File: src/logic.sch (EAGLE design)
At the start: 70 parts, among them CON1 CON-4P-TABS-JST_GH-RA, CON11 PINHEAD_1X04-2, CON12 PINHEAD_1X04-2, CON2 PINHEAD_1X04-2.54, CON3 PINHEAD_2X04-PLS-2, CON6 PINHEAD_2X02-PTH-2-MALE, CON7 PINHEAD_2X02-PTH-2-MALE, IC1 STM32F105RCT6, IC10 LM75-TSSOP8, IC11 LM75-TSSOP8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

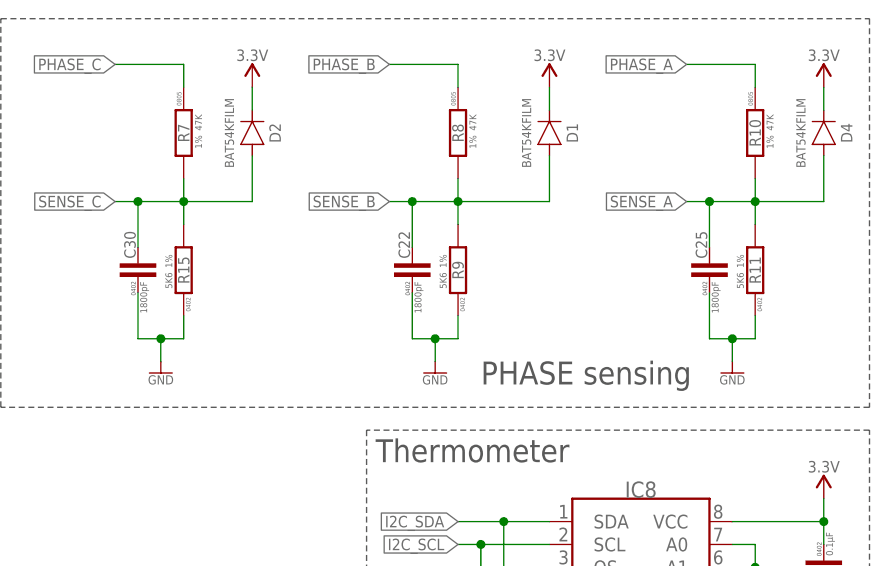
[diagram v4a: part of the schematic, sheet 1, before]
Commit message: phase sensing nominals updated
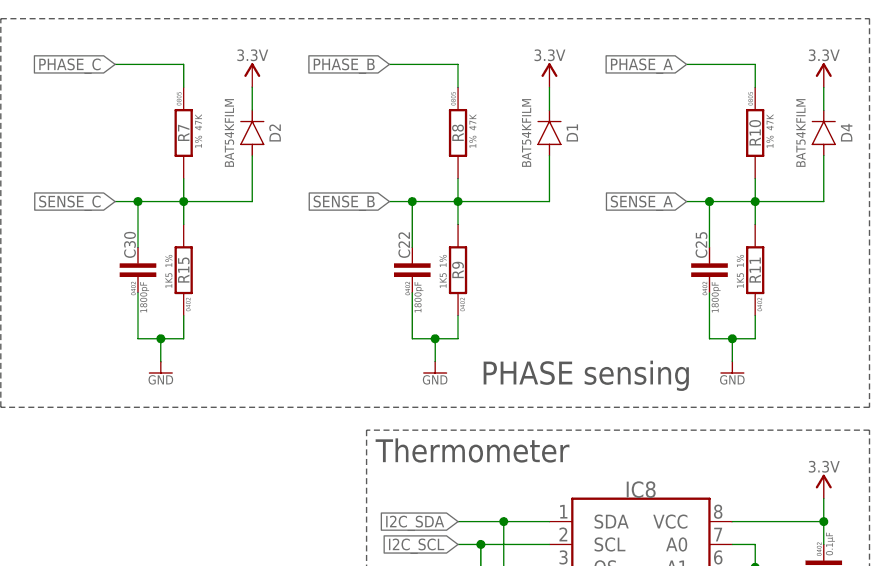
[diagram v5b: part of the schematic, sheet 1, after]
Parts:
- R11, R15, R9: value 5K6 -> 1K5
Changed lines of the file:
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@@
 <part name="C30" library="rc" library_urn="urn:adsk.eagle:library:2539423" deviceset="C" device="-0402" package3d_urn="urn:adsk.eagle:package:2539461/2" value="1800pF"/>
 <part name="R7" library="rc" library_urn="urn:adsk.eagle:library:2539423" deviceset="R" device="-0805" package3d_urn="urn:adsk.eagle:package:2539455/2" technology="-1%" value="47K"/>
-<part name="R15" library="rc" library_urn="urn:adsk.eagle:library:2539423" deviceset="R" device="-0402" package3d_urn="urn:adsk.eagle:package:2539456/2" technology="-1%" value="5K6"/>
+<part name="R15" library="rc" library_urn="urn:adsk.eagle:library:2539423" deviceset="R" device="-0402" package3d_urn="urn:adsk.eagle:package:2539456/2" technology="-1%" value="1K5"/>
 <part name="GND37" library="supply_symbols" library_urn="urn:adsk.eagle:library:13097679" deviceset="GND" device="" value="GND"/>
 <part name="C22" library="rc" library_urn="urn:adsk.eagle:library:2539423" deviceset="C" device="-0402" package3d_urn="urn:adsk.eagle:package:2539461/2" value="1800pF"/>
 <part name="R8" library="rc" library_urn="urn:adsk.eagle:library:2539423" deviceset="R" device="-0805" package3d_urn="urn:adsk.eagle:package:2539455/2" technology="-1%" value="47K"/>
-<part name="R9" library="rc" library_urn="urn:adsk.eagle:library:2539423" deviceset="R" device="-0402" package3d_urn="urn:adsk.eagle:package:2539456/2" technology="-1%" value="5K6"/>
+<part name="R9" library="rc" library_urn="urn:adsk.eagle:library:2539423" deviceset="R" device="-0402" package3d_urn="urn:adsk.eagle:package:2539456/2" technology="-1%" value="1K5"/>
 <part name="GND26" library="supply_symbols" library_urn="urn:adsk.eagle:library:13097679" deviceset="GND" device="" value="GND"/>
 <part name="C25" library="rc" library_urn="urn:adsk.eagle:library:2539423" deviceset="C" device="-0402" package3d_urn="urn:adsk.eagle:package:2539461/2" value="1800pF"/>
 <part name="R10" library="rc" library_urn="urn:adsk.eagle:library:2539423" deviceset="R" device="-0805" package3d_urn="urn:adsk.eagle:package:2539455/2" technology="-1%" value="47K"/>
-<part name="R11" library="rc" library_urn="urn:adsk.eagle:library:2539423" deviceset="R" device="-0402" package3d_urn="urn:adsk.eagle:package:2539456/2" technology="-1%" value="5K6"/>
+<part name="R11" library="rc" library_urn="urn:adsk.eagle:library:2539423" deviceset="R" device="-0402" package3d_urn="urn:adsk.eagle:package:2539456/2" technology="-1%" value="1K5"/>
 <part name="GND27" library="supply_symbols" library_urn="urn:adsk.eagle:library:13097679" deviceset="GND" device="" value="GND"/>
 <part name="+P7" library="supply_symbols" library_urn="urn:adsk.eagle:library:5017758" deviceset="3.3V" device=""/>

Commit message: Update logic.sch
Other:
- note added: "Max PHASE_x voltage should be around VDC_max VDC_max = 22 * 4.2 V = 92.4 V With resistor divider formed by 47K and 1K5 resistors SENSE_x max voltage is 92.4 * (1.5/(47+1.5)) = 2.85 V"
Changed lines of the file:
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@@
 Vref = 50*200*0.0002 =  2 V</text>
 <text x="106.68" y="218.44" size="1.27" layer="97" font="vector">Real Vref = 5.6/(5.6+3.3) * 3.3 = 2.07 V</text>
+<text x="218.44" y="248.92" size="1.778" layer="97" font="vector" align="center-left">Max PHASE_x voltage should  be around VDC_max
+VDC_max = 22 * 4.2 V = 92.4 V
+With resistor divider formed by 47K and 1K5 resistors
+SENSE_x max voltage is 92.4 * (1.5/(47+1.5)) = 2.85 V</text>
 </plain>
 <instances>

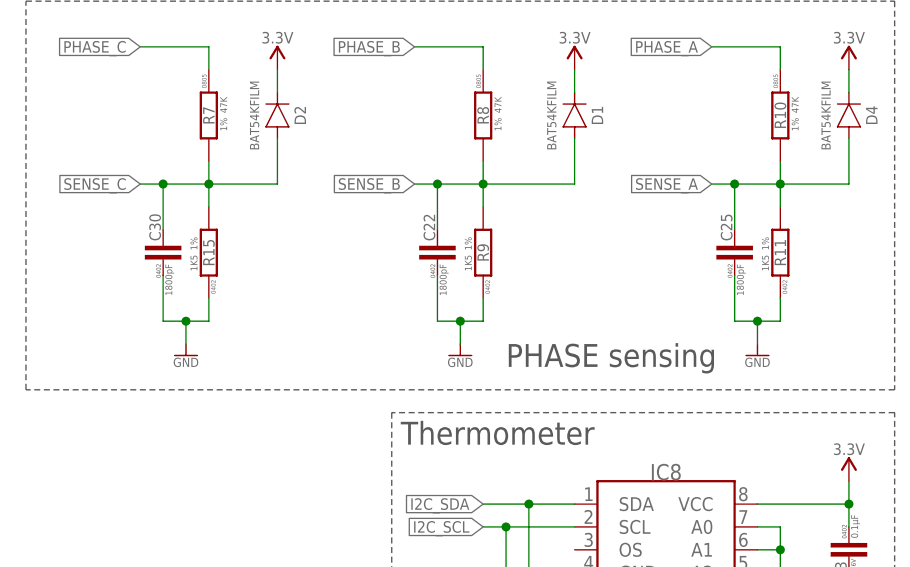
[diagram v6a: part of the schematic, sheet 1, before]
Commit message: Phase sensing filter update
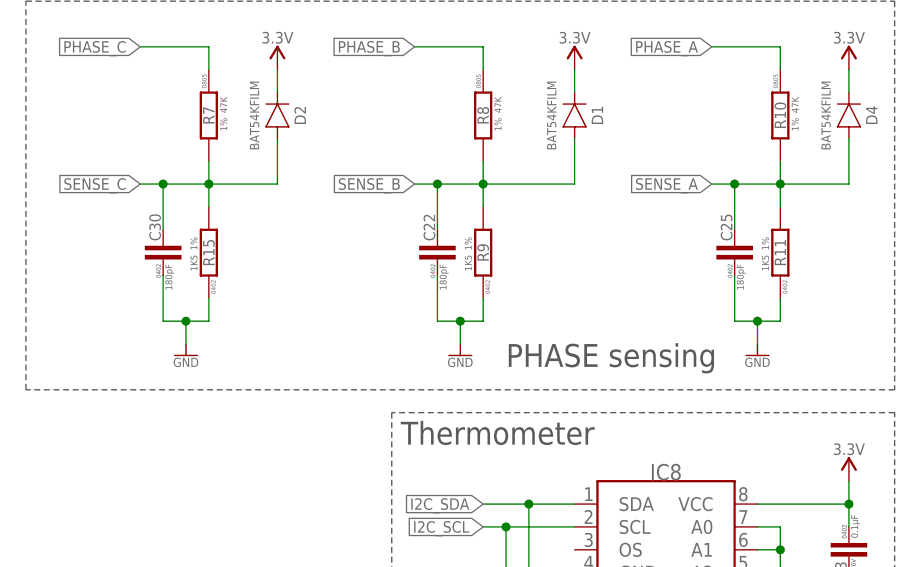
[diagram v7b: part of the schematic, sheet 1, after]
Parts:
- C22, C25, C30: value 1800pF -> 180pF
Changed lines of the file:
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@@
 <variant name="basic" populate="no"/>
 </part>
-<part name="C30" library="rc" library_urn="urn:adsk.eagle:library:2539423" deviceset="C" device="-0402" package3d_urn="urn:adsk.eagle:package:2539461/2" value="1800pF"/>
+<part name="C30" library="rc" library_urn="urn:adsk.eagle:library:2539423" deviceset="C" device="-0402" package3d_urn="urn:adsk.eagle:package:2539461/2" value="180pF"/>
 <part name="R7" library="rc" library_urn="urn:adsk.eagle:library:2539423" deviceset="R" device="-0805" package3d_urn="urn:adsk.eagle:package:2539455/2" technology="-1%" value="47K"/>
 <part name="R15" library="rc" library_urn="urn:adsk.eagle:library:2539423" deviceset="R" device="-0402" package3d_urn="urn:adsk.eagle:package:2539456/2" technology="-1%" value="1K5"/>
 <part name="GND37" library="supply_symbols" library_urn="urn:adsk.eagle:library:13097679" deviceset="GND" device="" value="GND"/>
-<part name="C22" library="rc" library_urn="urn:adsk.eagle:library:2539423" deviceset="C" device="-0402" package3d_urn="urn:adsk.eagle:package:2539461/2" value="1800pF"/>
+<part name="C22" library="rc" library_urn="urn:adsk.eagle:library:2539423" deviceset="C" device="-0402" package3d_urn="urn:adsk.eagle:package:2539461/2" value="180pF"/>
 <part name="R8" library="rc" library_urn="urn:adsk.eagle:library:2539423" deviceset="R" device="-0805" package3d_urn="urn:adsk.eagle:package:2539455/2" technology="-1%" value="47K"/>
 <part name="R9" library="rc" library_urn="urn:adsk.eagle:library:2539423" deviceset="R" device="-0402" package3d_urn="urn:adsk.eagle:package:2539456/2" technology="-1%" value="1K5"/>
 <part name="GND26" library="supply_symbols" library_urn="urn:adsk.eagle:library:13097679" deviceset="GND" device="" value="GND"/>
-<part name="C25" library="rc" library_urn="urn:adsk.eagle:library:2539423" deviceset="C" device="-0402" package3d_urn="urn:adsk.eagle:package:2539461/2" value="1800pF"/>
+<part name="C25" library="rc" library_urn="urn:adsk.eagle:library:2539423" deviceset="C" device="-0402" package3d_urn="urn:adsk.eagle:package:2539461/2" value="180pF"/>
 <part name="R10" library="rc" library_urn="urn:adsk.eagle:library:2539423" deviceset="R" device="-0805" package3d_urn="urn:adsk.eagle:package:2539455/2" technology="-1%" value="47K"/>
 <part name="R11" library="rc" library_urn="urn:adsk.eagle:library:2539423" deviceset="R" device="-0402" package3d_urn="urn:adsk.eagle:package:2539456/2" technology="-1%" value="1K5"/>

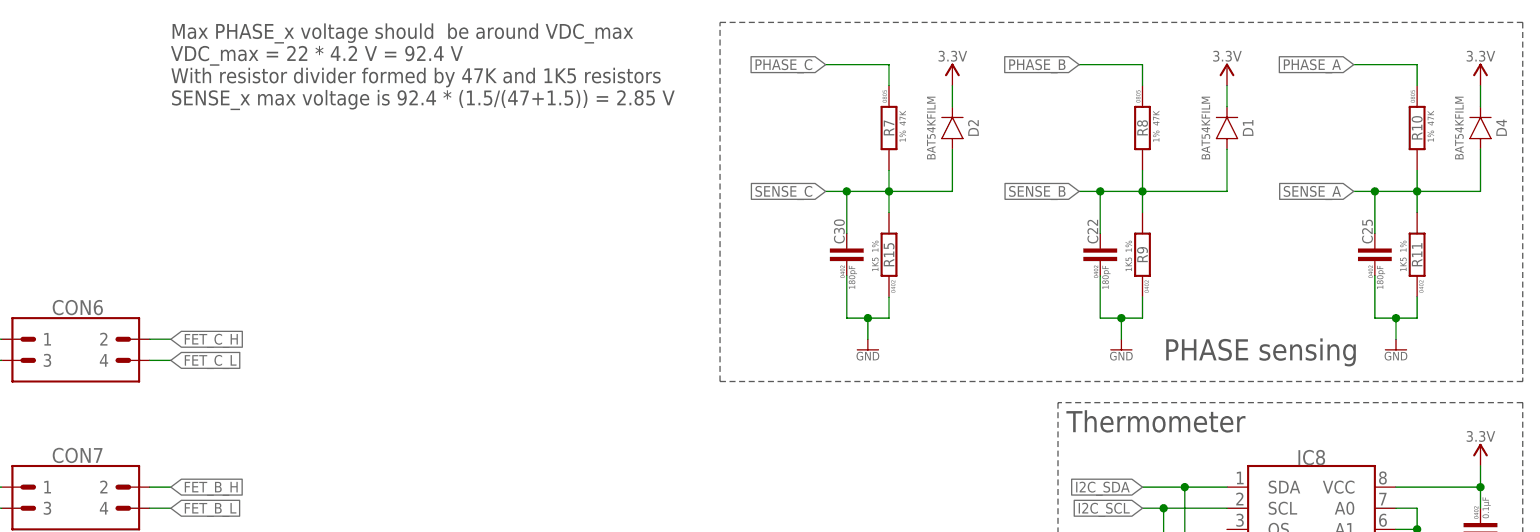
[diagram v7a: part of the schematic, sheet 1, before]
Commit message: BEMF filter update
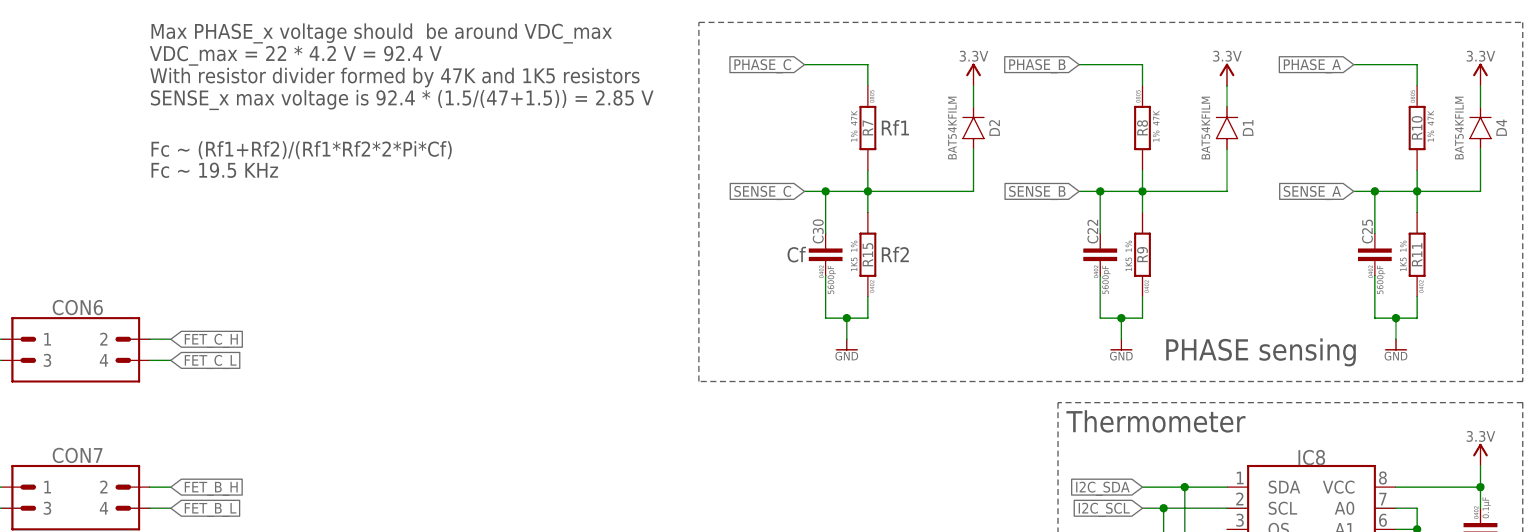
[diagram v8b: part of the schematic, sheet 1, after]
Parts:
- C22, C25, C30: value 180pF -> 5600pF
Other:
- note added: "Cf"
- note added: "Fc ~ (Rf1+Rf2)/(Rf1*Rf2*2*Pi*Cf)"
- note added: "Fc ~ 19.5 KHz"
- note added: "Rf1"
- note added: "Rf2"
- moved on the sheet: C30, D2, R15, R7
